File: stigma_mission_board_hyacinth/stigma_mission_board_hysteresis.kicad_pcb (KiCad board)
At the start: 4 copper layers, 50 x 150 mm, 209 parts, among them J10 Conn_02x02_Top_Bottom, J11 Conn_02x02_Top_Bottom, J12 Conn_02x02_Top_Bottom, J13 Conn_02x02_Top_Bottom, J2 Conn_02x05_Top_Bottom_Mountin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, J5 Conn_02x04_Top_Bottom, J6 Conn_02x04_Top_Bottom, J7 SMA, J8 SMA, J9 JST-GH 4Pin, Q1 DMN2056U, Q2 DMN2056U, Q3 AOSP21321, Q4 DMN2056U, Q5 AOSP21321, Q6 DMN2056U, Q7 AOSP21321, Q8 DMN2056U, Q9 AOSP21321, U1 LAN8742A, U10 MCP2562-E-SN, U11 MCP2562-E-SN, U12 SN74HCS594, U13 INA181, U14 INA181, U15 INA181, U16 INA181, U2 INA181, U3 TPD4E1U06, U4 L7805, U5 L7805, U6 AZ1117H-ADJ, U7 AZ1117H-ADJ, U8 Ai-Thinker-Ra-01, U9 Ai-Thinker-Ra-01, Y1 25MHz

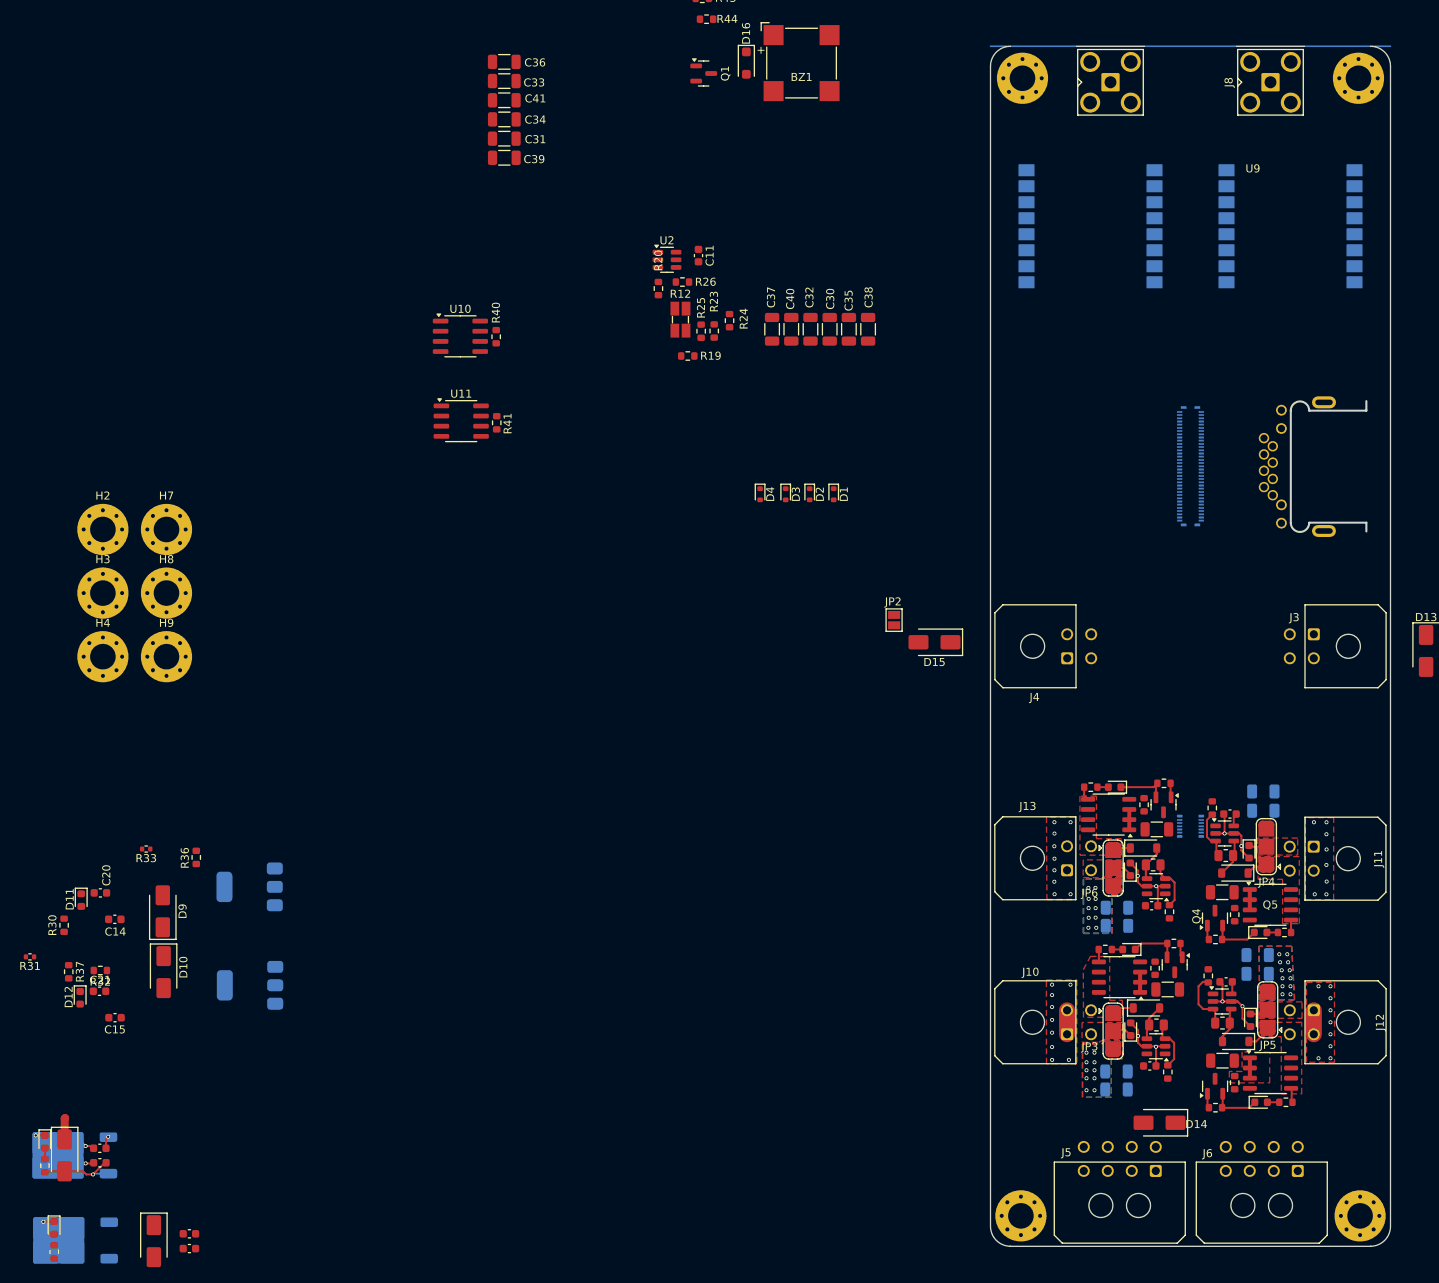
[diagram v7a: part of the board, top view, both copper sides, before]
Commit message: added GPS and Coreboard connector, changed ROs
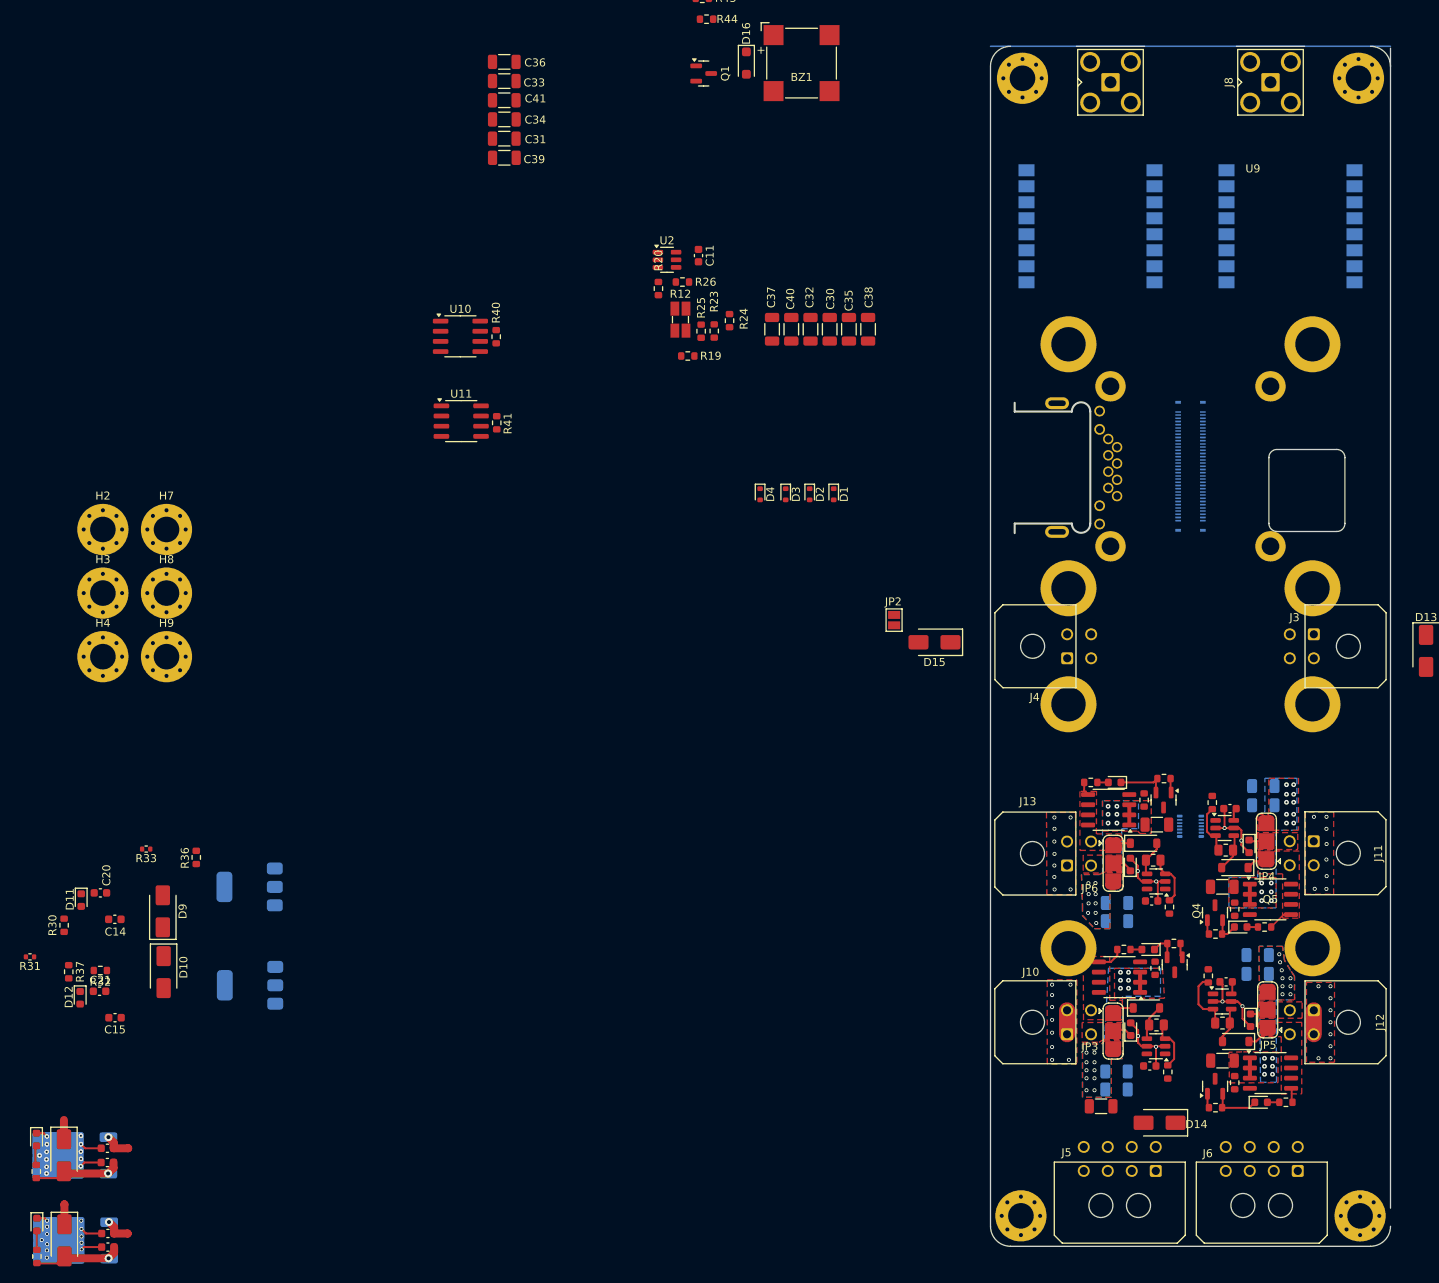
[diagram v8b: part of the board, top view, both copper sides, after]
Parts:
- J1: footprint Stigma:DF40GB-70DP-0.4V-plug -> Stigma:core-board
- J2: footprint Stigma:DF40GB-10DP-0.4V-plug -> Stigma:gps-board-outer-mounting-holes
- moved RJ1 25.9 mm to (212.1, 152.7), turned to 90 degrees
- moved C44 16.8 mm to (213.8, 232.5)
- moved D6 11.2 mm to (84.2, 249.3)
- moved C19 10.2 mm to (89.7, 250.1)
- moved C17 10.2 mm to (89.7, 248.4)
- moved R52 2.58 mm to (234.3, 210.1)
- moved D21 2.58 mm to (231.3, 210.1)
- moved D18 2.40 mm to (219.7, 212.9)
- moved R48 2.33 mm to (216.7, 212.9)
- moved R35 2.23 mm to (80.8, 251.3)
- moved D8 2.19 mm to (80.8, 247.3)
- moved R34 1.30 mm to (80.7, 240.7)
- moved D7 1.09 mm to (80.8, 236.7)
- moved C16 0.95 mm to (89.6, 237.8)
- moved C18 0.93 mm to (89.6, 239.5)
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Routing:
- net Net-(D6-A): track 0.00 -> 11.1 mm, vias 0 -> 1
- net main_voltage: track 1.55 -> 6.91 mm, vias 1 -> 2
- net Net-(D8-A): track 0.00 -> 2.40 mm
- net GND: track 76.8 -> 79.2 mm, vias 47 -> 67
- net +5V: track 2.72 -> 4.92 mm
- net /Recovery Output3/recovery_switched: track 3.82 -> 5.64 mm
- net /Recovery Output2/recovery_switched: track 4.18 -> 5.74 mm
- net Net-(D7-A): track 1.38 -> 2.49 mm
- net Net-(D5-A): track 10.4 -> 11.1 mm
- net /Recovery Output2/high_current: vias 0 -> 16
- net /Recovery Output3/high_current: vias 10 -> 16
- net /Recovery Output 4/high_current: vias 12 -> 15
- net /Recovery Output 1/high_current: vias 10 -> 15
- added copper zone on B.Cu, net /Recovery Output2/high_current
- added copper zone on F.Cu, net /Recovery Output2/high_current
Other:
- outline, holes or cut-outs redrawn
- board text added: "this one is not yet edited bc it's not yet clear whether we can remove the copper around the MP or not"
